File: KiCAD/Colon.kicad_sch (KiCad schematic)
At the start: 9 parts, among them J202 Output, U201 AZ1117-5.0

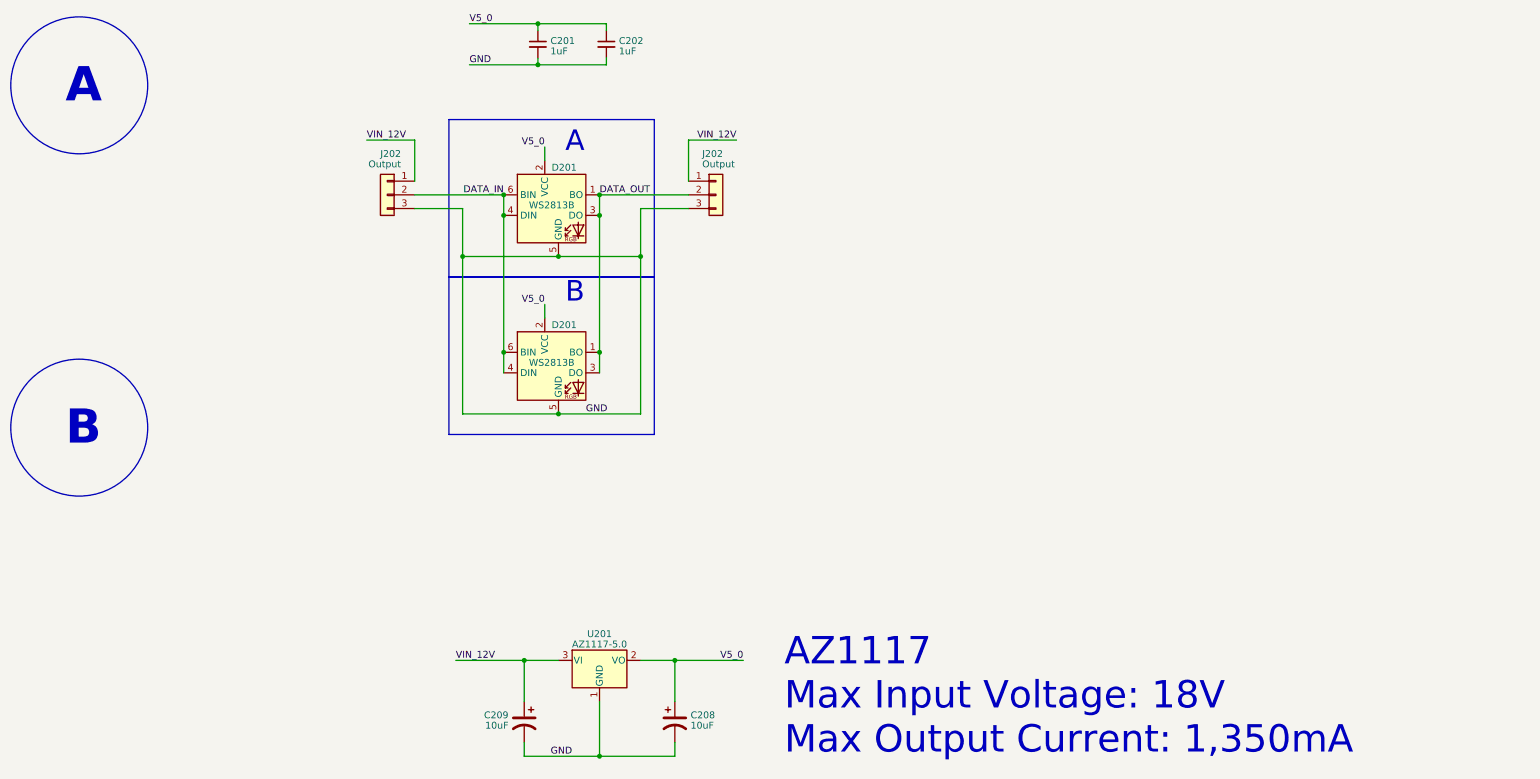
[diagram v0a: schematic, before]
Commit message: Initial PCB layout for 7-seg digits
I realize now that the PCB for the digits needs to be slanted, otherwise the colon pcb won't fit next to it, grumble
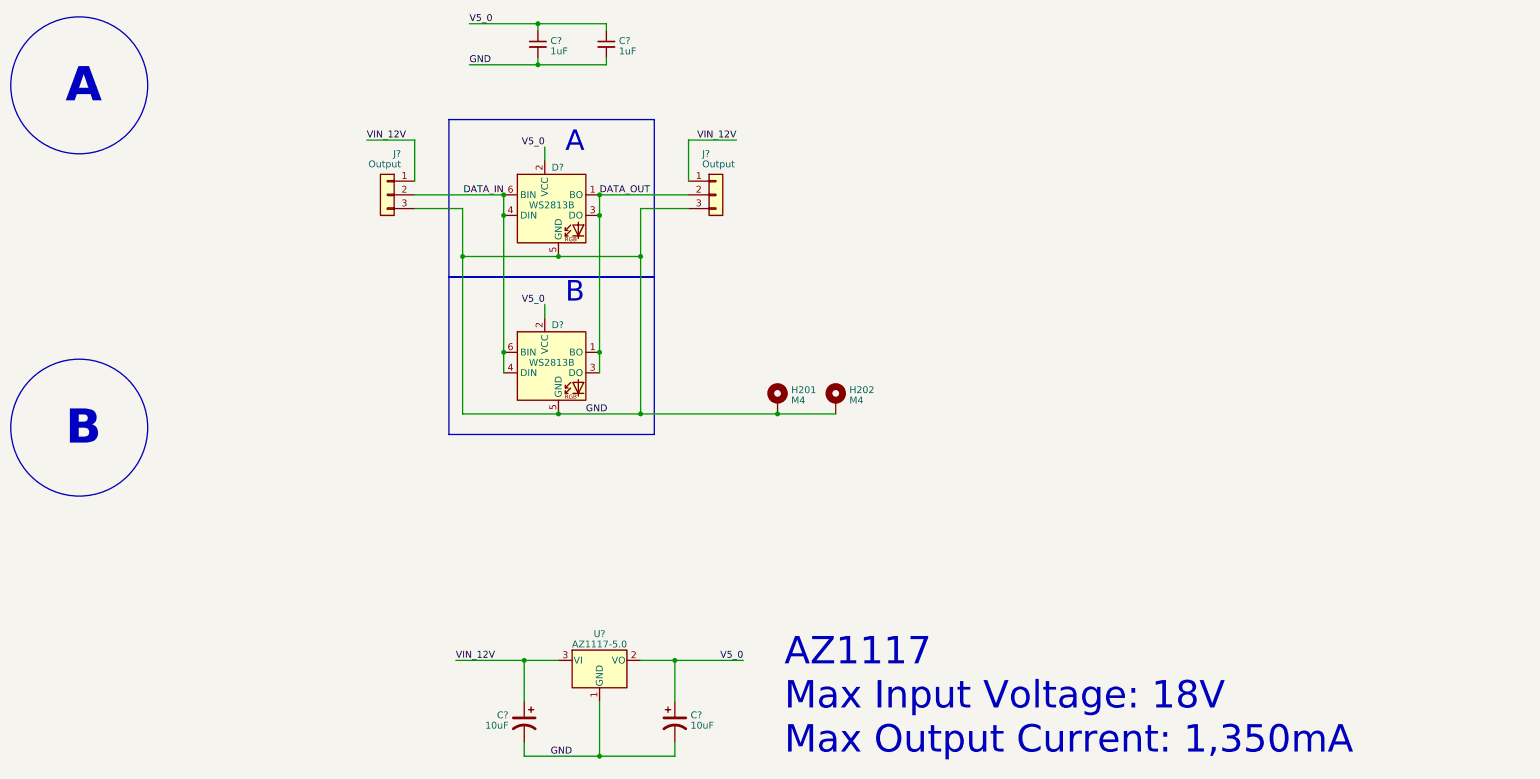
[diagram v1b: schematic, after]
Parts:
- added H201, H202: M4, MountingHole:MountingHole_4.3mm_M4_DIN965_Pad, symbol Mechanical:MountingHole_Pad
- C?: renamed from C202; footprint Capacitor_SMD:C_0402_1005Metric_Pad0.74x0.62mm_HandSolder -> Capacitor_SMD:C_0603_1608Metric_Pad1.08x0.95mm_HandSolder
- C?: renamed from C201; footprint Capacitor_SMD:C_0402_1005Metric_Pad0.74x0.62mm_HandSolder -> Capacitor_SMD:C_0603_1608Metric_Pad1.08x0.95mm_HandSolder
- renumbered C208 to C?, C209 to C?, D201 to D?, J202 to J?, U201 to U?
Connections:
- net GND: now also H201.1, H202.1
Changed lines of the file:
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@@
   (junction (at 147.32 187.96) (diameter 0) (color 0 0 0 1)
+  )
+  (junction (at 154.94 124.46) (diameter 0) (color 0 0 0 1)
+  )
+  (junction (at 180.34 124.46) (diameter 0) (color 0 0 0 1)
   )
   (junction (at 129.54 87.63) (diameter 0) (color 0 0 0 0)
@@
     (stroke (width 0) (type default))
   )
+  (wire (pts (xy 191.135 124.46) (xy 180.34 124.46))
+    (stroke (width 0) (type default) (color 0 0 0 1))
+  )
   (wire (pts (xy 121.92 86.36) (xy 121.92 95.25))
     (stroke (width 0) (type default) (color 0 0 0 1))
@@
   (wire (pts (xy 147.32 83.82) (xy 147.32 87.63))
     (stroke (width 0) (type default))
+  )
+  (wire (pts (xy 154.94 124.46) (xy 180.34 124.46))
+    (stroke (width 0) (type default) (color 0 0 0 1))
   )
   (wire (pts (xy 129.54 83.82) (xy 129.54 87.63))
@@
   (symbol (lib_id "Device:C_Polarized_US") (at 161.29 181.61 0) (unit 1)
     (in_bom yes) (on_board yes) (dnp no)
-    (property "Reference" "C208" (at 164.211 180.3313 0)
+    (property "Reference" "C?" (at 164.211 180.3313 0)
       (effects (font (size 1.27 1.27)) (justify left))
     )
@@
       (project "SevenSegClock-Main"
         (path "/2a5cec2f-c9dc-4298-92c3-7c4a8539120b/c210f423-f93a-431e-9b1d-29dff8886738"
-          (reference "C208") (unit 1)
+          (reference "C?") (unit 1)
         )
         (path "/2a5cec2f-c9dc-4298-92c3-7c4a8539120b/7800ca92-ebea-4cb9-8df4-5b5110cbd3d9"
-          (reference "C1102") (unit 1)
+          (reference "C304") (unit 1)
         )
       )
     )
   )
+  (symbol (lib_id "Mechanical:MountingHole_Pad") (at 191.135 121.92 0) (unit 1)
+    (in_bom yes) (on_board yes) (dnp no) (fields_autoplaced)
+    (property "Reference" "H202" (at 193.675 120.0063 0)
+      (effects (font (size 1.27 1.27)) (justify left))
+    )
+    (property "Value" "M4" (at 193.675 121.9273 0)
+      (effects (font (size 1.27 1.27)) (justify left))
+    )
+    (property "Footprint" "MountingHole:MountingHole_4.3mm_M4_DIN965_Pad" (at 191.135 121.92 0)
+      (effects (font (size 1.27 1.27)) hide)
+    )
+    (property "Datasheet" "~" (at 191.135 121.92 0)
+      (effects (font (size 1.27 1.27)) hide)
+    )
+    (pin "1")
+    (instances
+      (project "SevenSegClock-Main"
+        (path "/2a5cec2f-c9dc-4298-92c3-7c4a8539120b/c210f423-f93a-431e-9b1d-29dff8886738"
+          (reference "H202") (unit 1)
+        )
+        (path "/2a5cec2f-c9dc-4298-92c3-7c4a8539120b/7800ca92-ebea-4cb9-8df4-5b5110cbd3d9"
+          (reference "H302") (unit 1)
+        )
+      )
+    )
+  )
   (symbol (lib_id "Regulator_Linear:AZ1117-5.0") (at 147.32 170.18 0) (unit 1)
     (in_bom yes) (on_board yes) (dnp no) (fields_autoplaced)
-    (property "Reference" "U201" (at 147.32 165.2651 0)
+    (property "Reference" "U?" (at 147.32 165.2651 0)
       (effects (font (size 1.27 1.27)))
     )
@@
       (project "SevenSegClock-Main"
         (path "/2a5cec2f-c9dc-4298-92c3-7c4a8539120b/c210f423-f93a-431e-9b1d-29dff8886738"
-          (reference "U201") (unit 1)
+          (reference "U?") (unit 1)
         )
         (path "/2a5cec2f-c9dc-4298-92c3-7c4a8539120b/7800ca92-ebea-4cb9-8df4-5b5110cbd3d9"
-          (reference "U1101") (unit 1)
+          (reference "U301") (unit 1)
         )
       )
@@
   (symbol (lib_id "LEDs:WS2813B") (at 138.43 86.36 0) (unit 1)
     (in_bom yes) (on_board yes) (dnp no)
-    (property "Reference" "D201" (at 138.43 78.74 0)
+    (property "Reference" "D?" (at 138.43 78.74 0)
       (effects (font (size 1.27 1.27)) (justify left))
     )
@@
       (project "SevenSegClock-Main"
         (path "/2a5cec2f-c9dc-4298-92c3-7c4a8539120b/c210f423-f93a-431e-9b1d-29dff8886738"
-          (reference "D201") (unit 1)
+          (reference "D?") (unit 1)
         )
         (path "/2a5cec2f-c9dc-4298-92c3-7c4a8539120b/7800ca92-ebea-4cb9-8df4-5b5110cbd3d9"
-          (reference "D1101") (unit 1)
+          (reference "D301") (unit 1)
         )
       )
@@
   (symbol (lib_id "Device:C_Small") (at 148.59 55.88 0) (unit 1)
     (in_bom yes) (on_board yes) (dnp no) (fields_autoplaced)
-    (property "Reference" "C202" (at 150.9141 55.2426 0)
+    (property "Reference" "C?" (at 150.9141 55.2426 0)
       (effects (font (size 1.27 1.27)) (justify left))
     )
@@
       (effects (font (size 1.27 1.27)) (justify left))
     )
-    (property "Footprint" "Capacitor_SMD:C_0402_1005Metric_Pad0.74x0.62mm_HandSolder" (at 148.59 55.88 0)
+    (property "Footprint" "Capacitor_SMD:C_0603_1608Metric_Pad1.08x0.95mm_HandSolder" (at 148.59 55.88 0)
       (effects (font (size 1.27 1.27)) hide)
     )
@@
       (project "SevenSegClock-Main"
         (path "/2a5cec2f-c9dc-4298-92c3-7c4a8539120b/c210f423-f93a-431e-9b1d-29dff8886738"
-          (reference "C202") (unit 1)
+          (reference "C?") (unit 1)
         )
         (path "/2a5cec2f-c9dc-4298-92c3-7c4a8539120b/7800ca92-ebea-4cb9-8df4-5b5110cbd3d9"
-          (reference "C1104") (unit 1)
+          (reference "C303") (unit 1)
         )
       )
     )
   )
+  (symbol (lib_id "Mechanical:MountingHole_Pad") (at 180.34 121.92 0) (unit 1)
+    (in_bom yes) (on_board yes) (dnp no) (fields_autoplaced)
+    (property "Reference" "H201" (at 182.88 120.0063 0)
+      (effects (font (size 1.27 1.27)) (justify left))
+    )
+    (property "Value" "M4" (at 182.88 121.9273 0)
+      (effects (font (size 1.27 1.27)) (justify left))
+    )
+    (property "Footprint" "MountingHole:MountingHole_4.3mm_M4_DIN965_Pad" (at 180.34 121.92 0)
+      (effects (font (size 1.27 1.27)) hide)
+    )
+    (property "Datasheet" "~" (at 180.34 121.92 0)
+      (effects (font (size 1.27 1.27)) hide)
+    )
+    (pin "1")
+    (instances
+      (project "SevenSegClock-Main"
+        (path "/2a5cec2f-c9dc-4298-92c3-7c4a8539120b/c210f423-f93a-431e-9b1d-29dff8886738"
+          (reference "H201") (unit 1)
+        )
+        (path "/2a5cec2f-c9dc-4298-92c3-7c4a8539120b/7800ca92-ebea-4cb9-8df4-5b5110cbd3d9"
+          (reference "H301") (unit 1)
+        )
+      )
+    )
+  )
   (symbol (lib_id "LEDs:WS2813B") (at 138.43 115.57 0) (unit 1)
     (in_bom yes) (on_board yes) (dnp no)
-    (property "Reference" "D201" (at 138.43 107.95 0)
+    (property "Reference" "D?" (at 138.43 107.95 0)
       (effects (font (size 1.27 1.27)) (justify left))
     )
@@
       (project "SevenSegClock-Main"
         (path "/2a5cec2f-c9dc-4298-92c3-7c4a8539120b/c210f423-f93a-431e-9b1d-29dff8886738"
-          (reference "D201") (unit 1)
+          (reference "D?") (unit 1)
         )
         (path "/2a5cec2f-c9dc-4298-92c3-7c4a8539120b/7800ca92-ebea-4cb9-8df4-5b5110cbd3d9"
-          (reference "D1102") (unit 1)
+          (reference "D302") (unit 1)
         )
       )
@@
   (symbol (lib_id "Connector_Generic:Conn_01x03") (at 107.95 83.82 0) (mirror y) (unit 1)
     (in_bom yes) (on_board yes) (dnp no)
-    (property "Reference" "J202" (at 110.49 76.2 0)
+    (property "Reference" "J?" (at 110.49 76.2 0)
       (effects (font (size 1.27 1.27)) (justify left))
     )
@@
       (project "SevenSegClock-Main"
         (path "/2a5cec2f-c9dc-4298-92c3-7c4a8539120b/c210f423-f93a-431e-9b1d-29dff8886738"
-          (reference "J202") (unit 1)
+          (reference "J?") (unit 1)
         )
         (path "/2a5cec2f-c9dc-4298-92c3-7c4a8539120b/7800ca92-ebea-4cb9-8df4-5b5110cbd3d9"
-          (reference "J1102") (unit 1)
+          (reference "J301") (unit 1)
         )
       )
@@
   (symbol (lib_id "Connector_Generic:Conn_01x03") (at 168.91 83.82 0) (unit 1)
     (in_bom yes) (on_board yes) (dnp no)
-    (property "Reference" "J202" (at 166.37 76.2 0)
+    (property "Reference" "J?" (at 166.37 76.2 0)
       (effects (font (size 1.27 1.27)) (justify left))
     )
@@
       (project "SevenSegClock-Main"
         (path "/2a5cec2f-c9dc-4298-92c3-7c4a8539120b/c210f423-f93a-431e-9b1d-29dff8886738"
-          (reference "J202") (unit 1)
+          (reference "J?") (unit 1)
         )
         (path "/2a5cec2f-c9dc-4298-92c3-7c4a8539120b/7800ca92-ebea-4cb9-8df4-5b5110cbd3d9"
-          (reference "J1101") (unit 1)
+          (reference "J302") (unit 1)
         )
       )
@@
   (symbol (lib_id "Device:C_Polarized_US") (at 133.35 181.61 0) (mirror y) (unit 1)
     (in_bom yes) (on_board yes) (dnp no)
-    (property "Reference" "C209" (at 130.429 180.3313 0)
+    (property "Reference" "C?" (at 130.429 180.3313 0)
       (effects (font (size 1.27 1.27)) (justify left))
     )
@@
       (project "SevenSegClock-Main"
         (path "/2a5cec2f-c9dc-4298-92c3-7c4a8539120b/c210f423-f93a-431e-9b1d-29dff8886738"
-          (reference "C209") (unit 1)
+          (reference "C?") (unit 1)
         )
         (path "/2a5cec2f-c9dc-4298-92c3-7c4a8539120b/7800ca92-ebea-4cb9-8df4-5b5110cbd3d9"
-          (reference "C1101") (unit 1)
+          (reference "C301") (unit 1)
         )
       )
@@
   (symbol (lib_id "Device:C_Small") (at 135.89 55.88 0) (unit 1)
     (in_bom yes) (on_board yes) (dnp no) (fields_autoplaced)
-    (property "Reference" "C201" (at 138.2141 55.2426 0)
+    (property "Reference" "C?" (at 138.2141 55.2426 0)
       (effects (font (size 1.27 1.27)) (justify left))
     )
@@
       (effects (font (size 1.27 1.27)) (justify left))
     )
-    (property "Footprint" "Capacitor_SMD:C_0402_1005Metric_Pad0.74x0.62mm_HandSolder" (at 135.89 55.88 0)
+    (property "Footprint" "Capacitor_SMD:C_0603_1608Metric_Pad1.08x0.95mm_HandSolder" (at 135.89 55.88 0)
       (effects (font (size 1.27 1.27)) hide)
     )
@@
       (project "SevenSegClock-Main"
         (path "/2a5cec2f-c9dc-4298-92c3-7c4a8539120b/c210f423-f93a-431e-9b1d-29dff8886738"
-          (reference "C201") (unit 1)
+          (reference "C?") (unit 1)
         )
         (path "/2a5cec2f-c9dc-4298-92c3-7c4a8539120b/7800ca92-ebea-4cb9-8df4-5b5110cbd3d9"
-          (reference "C1103") (unit 1)
+          (reference "C302") (unit 1)
         )
       )
